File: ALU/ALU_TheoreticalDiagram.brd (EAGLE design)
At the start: 100 x 80 mm, 2 parts, among them IC2 74HC86D, U1 SN74LS283D

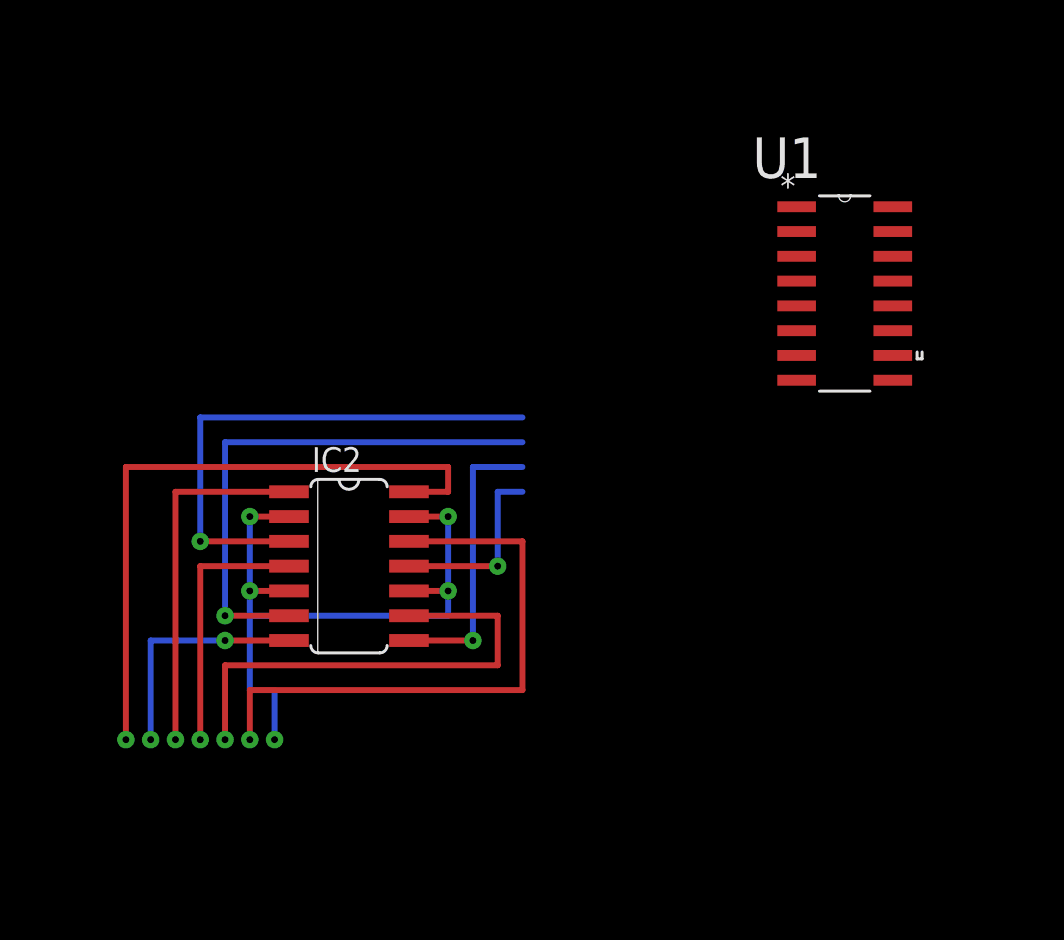
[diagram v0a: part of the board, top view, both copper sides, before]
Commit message: Added some routes
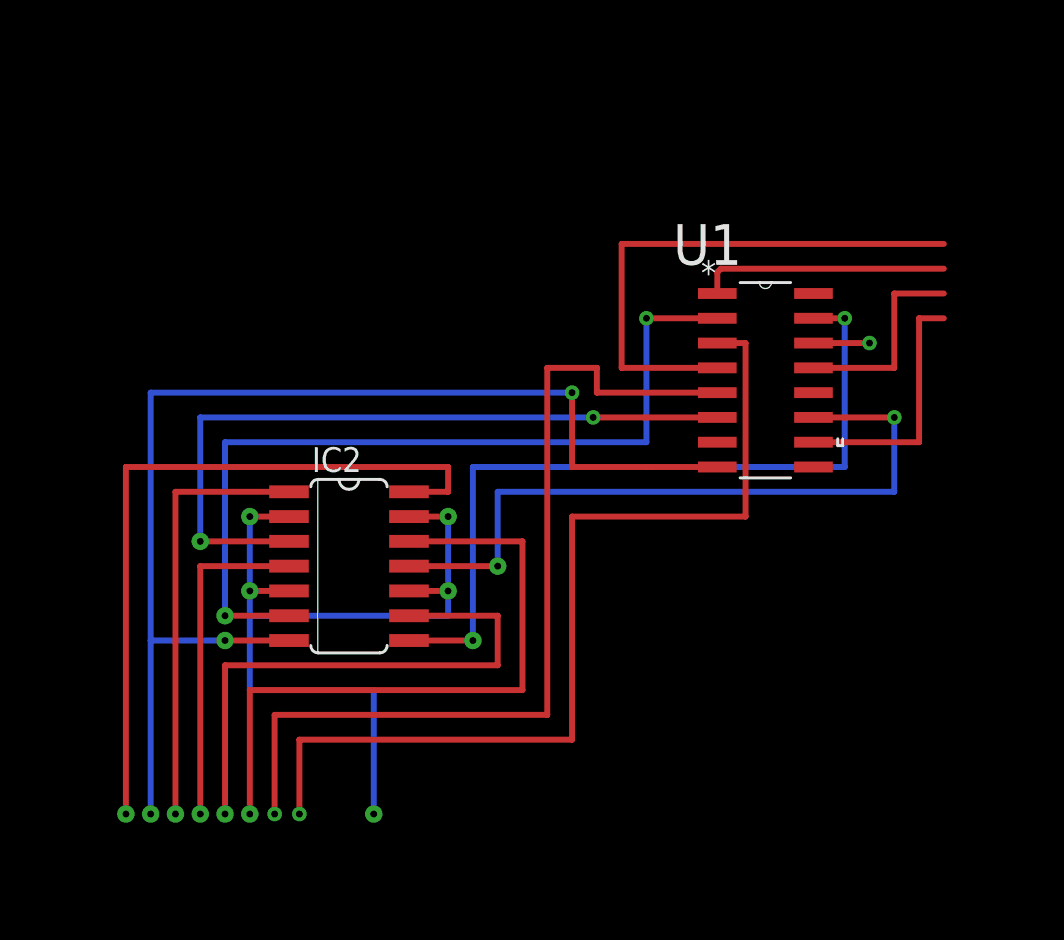
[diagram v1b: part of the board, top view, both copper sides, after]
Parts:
- moved U1 6.02 mm to (42.9, 34.9)
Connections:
- new net N$14: U1.8
- new net N$15: U1.16
- new net N$16: U1.4
- new net N$17: U1.1
- new net N$18: U1.13
- new net N$19: U1.10
- net VCC: no longer U1.16
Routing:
- net GND: track 12.2 -> 61.7 mm, vias 2 -> 3
- net N$12: track 0.00 -> 48.4 mm, vias 0 -> 1
- net N$13: track 0.00 -> 46.8 mm, vias 0 -> 1
- net N$16: track 0.00 -> 27.8 mm
- net N$9: track 9.63 -> 36.3 mm, vias 1 -> 2
- net N$8: track 14.7 -> 40.4 mm, vias 1 -> 2
- net N$7: track 27.4 -> 43.7 mm, vias 1 -> 2
- net N$19: track 0.00 -> 13.0 mm
- net N$17: track 0.00 -> 12.8 mm
- net N$18: track 0.00 -> 10.5 mm
- net N$10: track 27.4 -> 37.4 mm, vias 1 -> 2
- net N$5: track 36.0 -> 44.9 mm
- net N$4: track 29.9 -> 33.8 mm
- net N$2: track 13.4 -> 17.2 mm
- net VCC: track 33.8 -> 37.6 mm
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
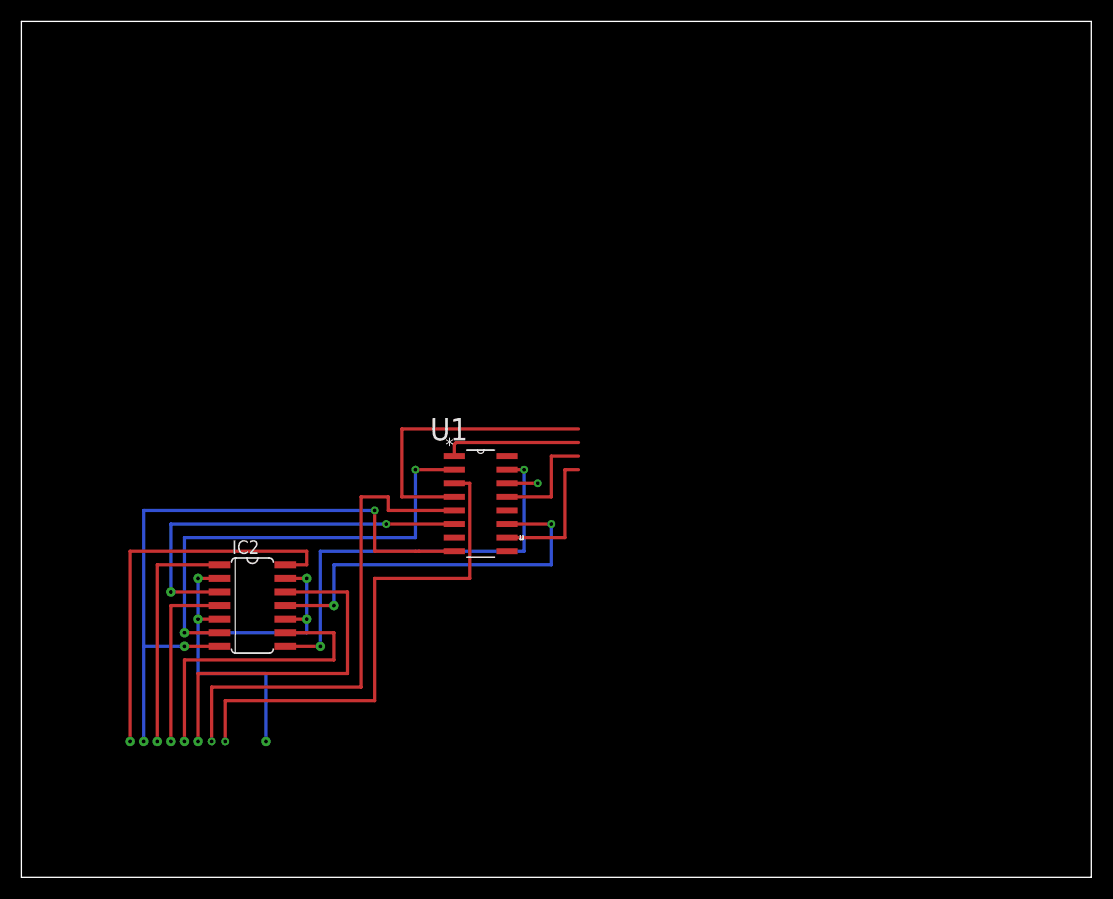
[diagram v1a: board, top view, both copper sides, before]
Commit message: Finished the ALU diagram
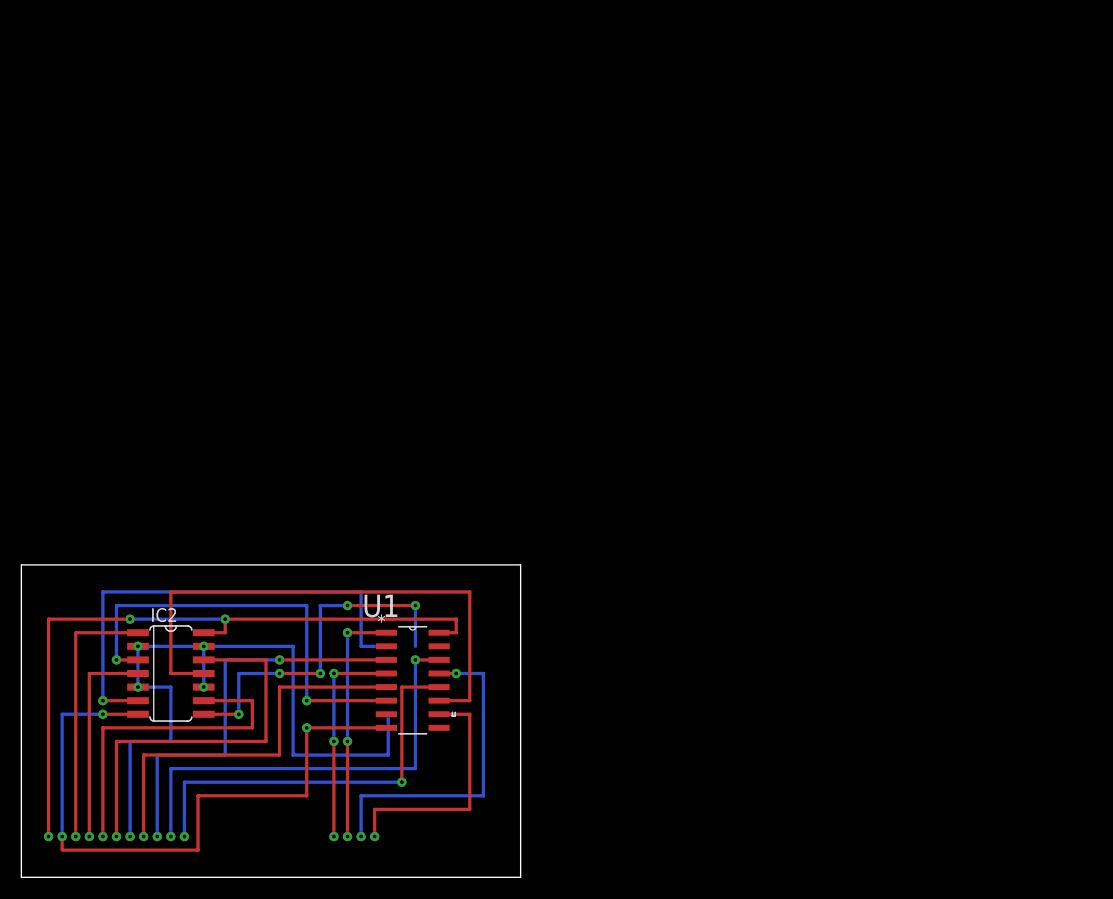
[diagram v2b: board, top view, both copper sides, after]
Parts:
- moved U1 17.7 mm to (36.6, 18.4)
- moved IC2 9.92 mm to (14.0, 19.1)
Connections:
- removed net N$15: U1.16
- net VCC: now also U1.16
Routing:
- net GND: track 61.7 -> 19.7 mm, vias 3 -> 2
- net N$14: track 0.00 -> 41.7 mm, vias 0 -> 1
- net N$6: track 2.87 -> 41.6 mm, vias 1 -> 2
- net N$11: track 0.00 -> 37.8 mm, vias 0 -> 2
- net VCC: track 37.6 -> 64.6 mm, vias 1 -> 3
- net N$5: track 44.9 -> 65.8 mm
- net N$18: track 10.5 -> 30.8 mm, vias 0 -> 2
- net N$9: track 36.3 -> 51.7 mm, vias 2 -> 0
- net N$12: track 48.4 -> 37.9 mm, vias 1 -> 2
- net N$13: track 46.8 -> 36.7 mm
- net N$19: track 13.0 -> 23.2 mm, vias 0 -> 1
- net N$17: track 12.8 -> 22.7 mm, vias 0 -> 3
- net N$16: track 27.8 -> 20.1 mm, vias 0 -> 3
- net N$8: track 40.4 -> 33.8 mm, vias 2 -> 5
- net N$10: track 37.4 -> 41.2 mm
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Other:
- board size 100 x 80 mm -> 46.7 x 29.2 mm
